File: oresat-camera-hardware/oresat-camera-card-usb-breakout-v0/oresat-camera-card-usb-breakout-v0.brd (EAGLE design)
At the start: 44 x 29 mm, 4 parts, among them J2 USB_A_SMT_FEMALE, J3 2-1734592-0

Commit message: first draft finished
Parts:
- added TP1: TEST-POINTPOGO_PTH, SparkFun-Connectors:1X01_NO_SILK
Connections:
- new net N$2: J3.17, TP1.1
- net GND: no longer J3.17
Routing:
- net N$2: track 0.00 -> 11.3 mm
- net GND: track 19.4 -> 17.4 mm, vias 49 -> 48
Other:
- board text added: "HOST ID"
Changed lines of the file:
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@@
 <text x="8.75" y="7.375" size="1" layer="21" font="vector" ratio="20">CLIENT</text>
 <text x="28.375" y="17.25" size="1" layer="21" font="vector" ratio="20">HOST</text>
+<text x="32.5" y="21.75" size="1" layer="21" font="vector" ratio="20">HOST ID</text>
 </plain>
 <attributes>
@@
 <attribute name="NAME" x="18" y="3" size="0.3" layer="33" ratio="15" rot="R270" align="center"/>
 </element>
+<element name="TP1" library="SparkFun-Connectors" package="1X01_NO_SILK" value="TEST-POINTPOGO_PTH" x="35" y="20" smashed="yes">
+<attribute name="NAME" x="36.48" y="19.768" size="0.6096" layer="25" font="vector" ratio="20"/>
+</element>
 </elements>
 <signals>
@@
 <contactref element="J3" pad="10"/>
 <contactref element="J3" pad="14"/>
-<contactref element="J3" pad="17"/>
 <contactref element="J3" pad="S1"/>
 <contactref element="J3" pad="S2"/>
@@
 <via x="13.875" y="24" extent="1-16" drill="0.35"/>
 <via x="15.625" y="26.125" extent="1-16" drill="0.35"/>
-<via x="25.5" y="23.3125" extent="1-16" drill="0.35"/>
+<via x="25.75" y="23.3125" extent="1-16" drill="0.35"/>
 <via x="26.5" y="23.3125" extent="1-16" drill="0.35"/>
 <via x="28.4375" y="21.75" extent="1-16" drill="0.35"/>
 <via x="30.1875" y="23.9375" extent="1-16" drill="0.35"/>
 <via x="28.4375" y="26" extent="1-16" drill="0.35"/>
-<via x="25.5" y="21.0625" extent="1-16" drill="0.35"/>
 <via x="26.5625" y="21.0625" extent="1-16" drill="0.35"/>
 <via x="32.5625" y="14.3125" extent="1-16" drill="0.35"/>
@@
 <via x="21" y="6" extent="1-16" drill="0.35"/>
 <via x="19" y="9" extent="1-16" drill="0.35"/>
-<via x="31" y="20" extent="1-16" drill="0.35"/>
+<via x="32" y="19" extent="1-16" drill="0.35"/>
 <via x="30" y="10" extent="1-16" drill="0.35"/>
 <via x="30" y="3" extent="1-16" drill="0.35"/>
@@
 <wire x1="26.268" y1="22.225" x2="26.268" y2="23.0805" width="0.254" layer="1"/>
 <wire x1="26.268" y1="23.0805" x2="26.5" y2="23.3125" width="0.254" layer="1"/>
-<wire x1="25.768" y1="22.225" x2="25.768" y2="23.0445" width="0.254" layer="1"/>
-<wire x1="25.768" y1="23.0445" x2="25.5" y2="23.3125" width="0.254" layer="1"/>
-<wire x1="25.268" y1="22.225" x2="25.268" y2="23.0805" width="0.254" layer="1"/>
-<wire x1="25.268" y1="23.0805" x2="25.5" y2="23.3125" width="0.254" layer="1"/>
 <wire x1="21.768" y1="22.225" x2="21.768" y2="23.0805" width="0.254" layer="1"/>
 <wire x1="21.768" y1="23.0805" x2="22" y2="23.3125" width="0.254" layer="1"/>
@@
 <wire x1="12.3" y1="5.6125" x2="12.5" y2="5.8125" width="0.254" layer="1"/>
 <contactref element="C1" pad="1"/>
-<wire x1="25.268" y1="22.225" x2="25.268" y2="21.2945" width="0.254" layer="1"/>
-<wire x1="25.268" y1="21.2945" x2="25.5" y2="21.0625" width="0.254" layer="1"/>
 <wire x1="25.768" y1="22.225" x2="25.768" y2="21.3305" width="0.254" layer="1"/>
-<wire x1="25.768" y1="21.3305" x2="25.5" y2="21.0625" width="0.254" layer="1"/>
 <wire x1="26.268" y1="22.225" x2="26.268" y2="21.357" width="0.254" layer="1"/>
 <wire x1="26.268" y1="21.357" x2="26.5625" y2="21.0625" width="0.254" layer="1"/>
 <wire x1="26.768" y1="22.225" x2="26.768" y2="21.268" width="0.254" layer="1"/>
 <wire x1="26.768" y1="21.268" x2="26.5625" y2="21.0625" width="0.254" layer="1"/>
+<wire x1="25.75" y1="23.3125" x2="25.768" y2="23.2945" width="0.254" layer="1"/>
+<wire x1="25.768" y1="23.2945" x2="25.768" y2="22.225" width="0.254" layer="1"/>
+<wire x1="25.768" y1="21.3305" x2="26.036" y2="21.0625" width="0.254" layer="1"/>
+<wire x1="26.036" y1="21.0625" x2="26.5625" y2="21.0625" width="0.254" layer="1"/>
+<wire x1="33" y1="26" x2="37" y2="26" width="0" layer="19" extent="1-1"/>
+<wire x1="30.1875" y1="23.9375" x2="33" y2="26" width="0" layer="19" extent="1-1"/>
+<wire x1="28.438" y1="23.925" x2="30.1875" y2="23.9375" width="0" layer="19" extent="1-1"/>
+<wire x1="26.5" y1="23.3125" x2="28.438" y2="23.925" width="0" layer="19" extent="1-1"/>
+<wire x1="28.4375" y1="21.75" x2="26.768" y2="22.225" width="0" layer="19" extent="1-1"/>
+<wire x1="23.75" y1="23.3125" x2="25.75" y2="23.3125" width="0" layer="19" extent="1-1"/>
+<wire x1="22.268" y1="22.225" x2="23.768" y2="22.225" width="0" layer="19" extent="1-1"/>
+<wire x1="20.768" y1="22.225" x2="21.768" y2="22.225" width="0" layer="19" extent="1-1"/>
+<wire x1="19.25" y1="23.3125" x2="20.75" y2="23.3125" width="0" layer="19" extent="1-1"/>
+<wire x1="17.768" y1="22.225" x2="19.268" y2="22.225" width="0" layer="19" extent="1-1"/>
+<wire x1="17.375" y1="24.1875" x2="17.5" y2="23.3125" width="0" layer="19" extent="1-1"/>
+<wire x1="15.625" y1="21.8125" x2="17.268" y2="22.225" width="0" layer="19" extent="1-1"/>
+<wire x1="15.598" y1="23.925" x2="17.375" y2="24.1875" width="0" layer="19" extent="1-1"/>
+<wire x1="13.875" y1="24" x2="15.598" y2="23.925" width="0" layer="19" extent="1-1"/>
+<wire x1="28.4375" y1="26" x2="28.438" y2="23.925" width="0" layer="19" extent="1-1"/>
+<wire x1="15.625" y1="26.125" x2="15.598" y2="23.925" width="0" layer="19" extent="1-1"/>
+<wire x1="14" y1="20" x2="15.625" y2="21.8125" width="0" layer="19" extent="1-1"/>
+<wire x1="11.5" y1="17.875" x2="14" y2="20" width="0" layer="19" extent="1-1"/>
+<wire x1="10" y1="16" x2="11.5" y2="17.875" width="0" layer="19" extent="1-1"/>
+<wire x1="11" y1="26" x2="13.875" y2="24" width="0" layer="19" extent="1-1"/>
+<wire x1="8" y1="13" x2="10" y2="16" width="0" layer="19" extent="1-1"/>
+<wire x1="6" y1="12" x2="8" y2="13" width="0" layer="19" extent="1-1"/>
+<wire x1="5" y1="9" x2="6" y2="12" width="0" layer="19" extent="1-1"/>
+<wire x1="3" y1="7" x2="5" y2="9" width="0" layer="19" extent="1-1"/>
+<wire x1="5" y1="6" x2="3" y2="7" width="0" layer="19" extent="1-1"/>
+<wire x1="7" y1="26" x2="11" y2="26" width="0" layer="19" extent="1-1"/>
+<wire x1="3" y1="15" x2="6" y2="12" width="0" layer="19" extent="1-1"/>
+<wire x1="32" y1="19" x2="28.4375" y2="21.75" width="0" layer="19" extent="1-1"/>
+<wire x1="33.5" y1="16.3125" x2="32" y2="19" width="0" layer="19" extent="1-1"/>
+<wire x1="35" y1="17" x2="33.5" y2="16.3125" width="0" layer="19" extent="1-1"/>
+<wire x1="33.5" y1="14.212" x2="33.5" y2="16.3125" width="0" layer="19" extent="1-1"/>
+<wire x1="32.5625" y1="14.3125" x2="33.5" y2="14.212" width="0" layer="19" extent="1-1"/>
+<wire x1="34.5" y1="14.3125" x2="33.5" y2="14.212" width="0" layer="19" extent="1-1"/>
+<wire x1="33.5" y1="12.0625" x2="33.5" y2="14.212" width="0" layer="19" extent="1-1"/>
+<wire x1="36.5659" y1="10" x2="33.5" y2="12.0625" width="0" layer="19" extent="1-1"/>
+<wire x1="30" y1="10" x2="33.5" y2="12.0625" width="0" layer="19" extent="1-1"/>
+<wire x1="41" y1="7" x2="36.5659" y2="10" width="0" layer="19" extent="1-1"/>
+<wire x1="41" y1="22" x2="37" y2="26" width="0" layer="19" extent="1-1"/>
+<wire x1="3" y1="22" x2="7" y2="26" width="0" layer="19" extent="1-1"/>
+<wire x1="41" y1="15" x2="35" y2="17" width="0" layer="19" extent="1-1"/>
+<wire x1="23.4341" y1="10" x2="30" y2="10" width="0" layer="19" extent="1-1"/>
+<wire x1="19" y1="9" x2="23.4341" y2="10" width="0" layer="19" extent="1-1"/>
+<wire x1="18" y1="12" x2="19" y2="9" width="0" layer="19" extent="1-1"/>
+<wire x1="20" y1="14" x2="18" y2="12" width="0" layer="19" extent="1-1"/>
+<wire x1="16" y1="10" x2="18" y2="12" width="0" layer="19" extent="1-1"/>
+<wire x1="14" y1="8" x2="16" y2="10" width="0" layer="19" extent="1-1"/>
+<wire x1="12.5" y1="5.8125" x2="14" y2="8" width="0" layer="19" extent="1-1"/>
+<wire x1="21" y1="6" x2="19" y2="9" width="0" layer="19" extent="1-1"/>
+<wire x1="18" y1="5" x2="21" y2="6" width="0" layer="19" extent="1-1"/>
+<wire x1="18" y1="3.9" x2="18" y2="5" width="0" layer="19" extent="1-1"/>
+<wire x1="30" y1="3" x2="30" y2="10" width="0" layer="19" extent="1-1"/>
 </signal>
 <signal name="CLIENT_VBUS">
@@
 <wire x1="7" y1="1.5" x2="9.8" y2="1.5" width="0" layer="19" extent="1-1"/>
 </signal>
+<signal name="N$2">
+<contactref element="J3" pad="17"/>
+<contactref element="TP1" pad="1"/>
+<wire x1="25.268" y1="22.225" x2="25.3894" y2="22.1036" width="0.1524" layer="1"/>
+<wire x1="25.3894" y1="22.1036" x2="25.3894" y2="21.0812" width="0.1524" layer="1"/>
+<wire x1="25.3894" y1="21.0812" x2="26.4706" y2="20" width="0.1524" layer="1"/>
+<wire x1="26.4706" y1="20" x2="35" y2="20" width="0.1524" layer="1"/>
+</signal>
 </signals>

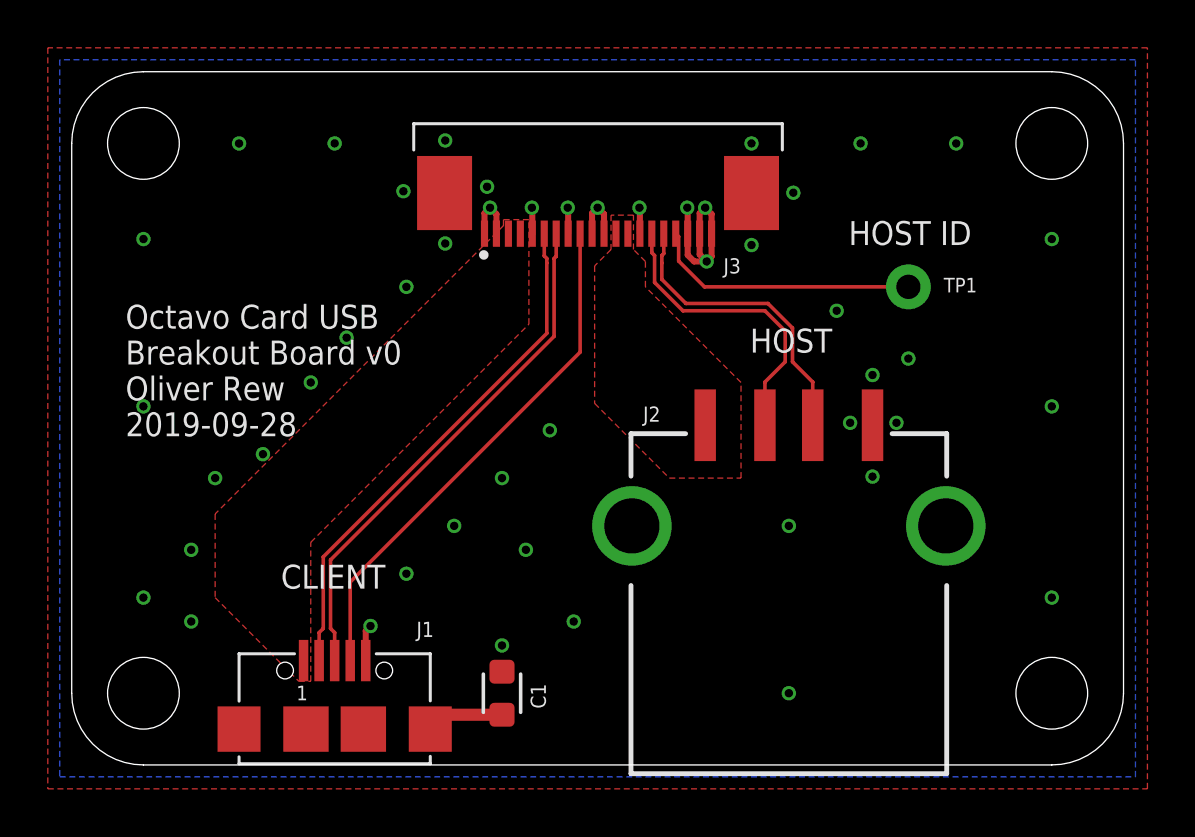
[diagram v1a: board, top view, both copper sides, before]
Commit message: added VDD caps
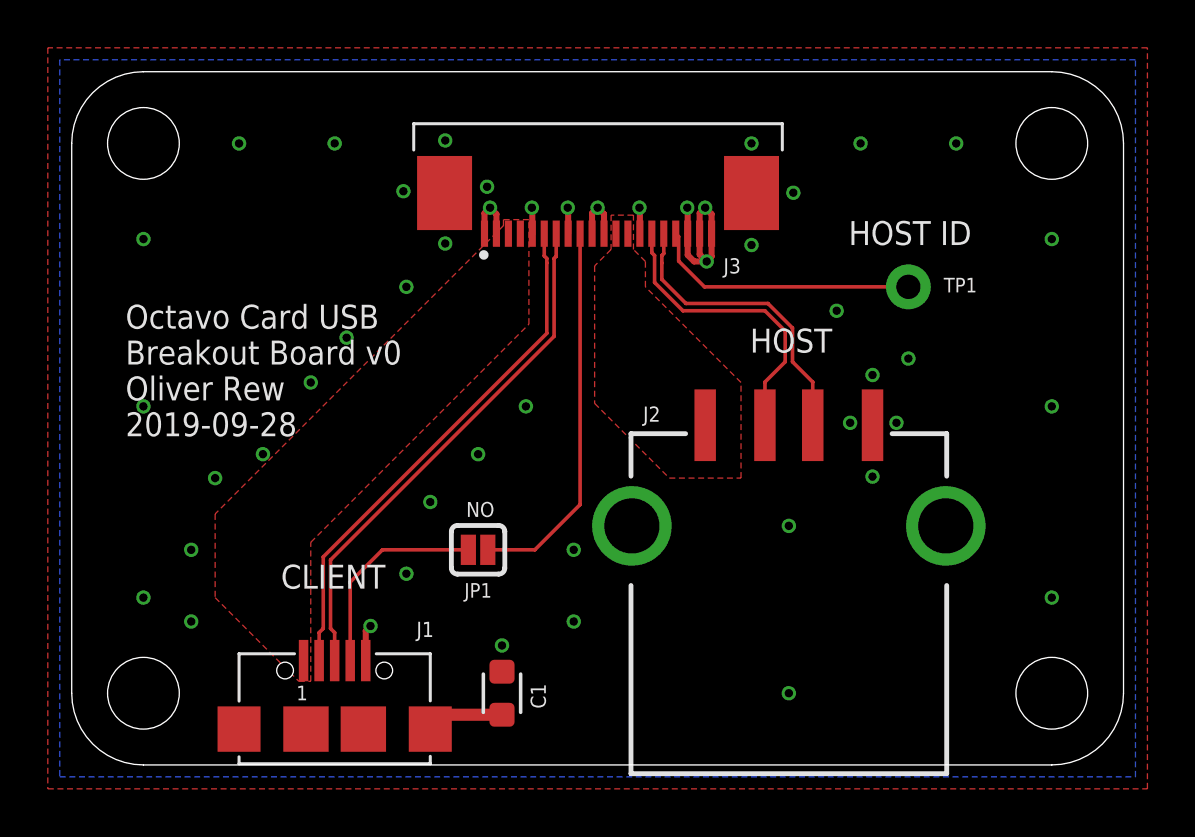
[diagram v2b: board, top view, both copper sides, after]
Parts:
- added JP1: JUMPER-SMT_2_NO_SILK, SparkFun-Jumpers:SMT-JUMPER_2_NO_SILK
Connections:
- new net N$3: J1.4, JP1.2
- net N$5: now also JP1.1; no longer J1.4
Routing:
- net N$3: track 0.00 -> 8.79 mm
- net N$5: track 21.8 -> 16.0 mm
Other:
- board text added: "NO"
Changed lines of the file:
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@@
 <?xml version="1.0" encoding="utf-8"?>
 <!DOCTYPE eagle SYSTEM "eagle.dtd">
-<eagle version="9.5.0">
+<eagle version="9.4.2">
 <drawing>
 <settings>
@@
 <text x="28.375" y="17.25" size="1" layer="21" font="vector" ratio="20">HOST</text>
 <text x="32.5" y="21.75" size="1" layer="21" font="vector" ratio="20">HOST ID</text>
+<text x="16.5" y="10.375" size="0.625" layer="21" font="vector" ratio="20">NO</text>
 </plain>
 <attributes>
@@
 <attribute name="NAME" x="36.48" y="19.768" size="0.6096" layer="25" font="vector" ratio="20"/>
 </element>
+<element name="JP1" library="SparkFun-Jumpers" package="SMT-JUMPER_2_NO_SILK" value="JUMPER-SMT_2_NO_SILK" x="17" y="9" smashed="yes" rot="R180">
+<attribute name="NAME" x="17" y="7.607" size="0.6096" layer="25" font="vector" ratio="20" rot="R180" align="bottom-center"/>
+</element>
 </elements>
 <signals>
@@
 <via x="14" y="20" extent="1-16" drill="0.35"/>
 <via x="14" y="8" extent="1-16" drill="0.35"/>
-<via x="16" y="10" extent="1-16" drill="0.35"/>
-<via x="18" y="12" extent="1-16" drill="0.35"/>
-<via x="20" y="14" extent="1-16" drill="0.35"/>
+<via x="15" y="11" extent="1-16" drill="0.35"/>
+<via x="17" y="13" extent="1-16" drill="0.35"/>
+<via x="19" y="15" extent="1-16" drill="0.35"/>
 <via x="35" y="17" extent="1-16" drill="0.35"/>
 <via x="37" y="26" extent="1-16" drill="0.35"/>
@@
 <via x="18" y="5" extent="1-16" drill="0.35"/>
 <via x="21" y="6" extent="1-16" drill="0.35"/>
-<via x="19" y="9" extent="1-16" drill="0.35"/>
+<via x="21" y="9" extent="1-16" drill="0.35"/>
 <via x="32" y="19" extent="1-16" drill="0.35"/>
 <via x="30" y="10" extent="1-16" drill="0.35"/>
@@
 <wire x1="41" y1="15" x2="35" y2="17" width="0" layer="19" extent="1-1"/>
 <wire x1="23.4341" y1="10" x2="30" y2="10" width="0" layer="19" extent="1-1"/>
-<wire x1="19" y1="9" x2="23.4341" y2="10" width="0" layer="19" extent="1-1"/>
-<wire x1="18" y1="12" x2="19" y2="9" width="0" layer="19" extent="1-1"/>
-<wire x1="20" y1="14" x2="18" y2="12" width="0" layer="19" extent="1-1"/>
-<wire x1="16" y1="10" x2="18" y2="12" width="0" layer="19" extent="1-1"/>
-<wire x1="14" y1="8" x2="16" y2="10" width="0" layer="19" extent="1-1"/>
+<wire x1="21" y1="9" x2="23.4341" y2="10" width="0" layer="19" extent="1-1"/>
+<wire x1="17" y1="13" x2="21" y2="9" width="0" layer="19" extent="1-1"/>
+<wire x1="19" y1="15" x2="17" y2="13" width="0" layer="19" extent="1-1"/>
+<wire x1="15" y1="11" x2="17" y2="13" width="0" layer="19" extent="1-1"/>
+<wire x1="14" y1="8" x2="15" y2="11" width="0" layer="19" extent="1-1"/>
 <wire x1="12.5" y1="5.8125" x2="14" y2="8" width="0" layer="19" extent="1-1"/>
-<wire x1="21" y1="6" x2="19" y2="9" width="0" layer="19" extent="1-1"/>
+<wire x1="21" y1="6" x2="21" y2="9" width="0" layer="19" extent="1-1"/>
 <wire x1="18" y1="5" x2="21" y2="6" width="0" layer="19" extent="1-1"/>
 <wire x1="18" y1="3.9" x2="18" y2="5" width="0" layer="19" extent="1-1"/>
@@
 <signal name="N$5">
 <contactref element="J3" pad="9"/>
-<contactref element="J1" pad="4"/>
-<wire x1="11.65" y1="4.3655" x2="11.65" y2="7.65" width="0.1524" layer="1"/>
-<wire x1="21.268" y1="17.268" x2="21.268" y2="22.225" width="0.1524" layer="1"/>
-<wire x1="11.65" y1="7.65" x2="21.268" y2="17.268" width="0.1524" layer="1"/>
+<contactref element="JP1" pad="1"/>
+<wire x1="17.4064" y1="9" x2="19.375" y2="9" width="0.1524" layer="1"/>
+<wire x1="19.375" y1="9" x2="21.268" y2="10.893" width="0.1524" layer="1"/>
+<wire x1="21.268" y1="10.893" x2="21.268" y2="22.225" width="0.1524" layer="1"/>
 </signal>
 <signal name="HOST_VBUS">
@@
 <wire x1="26.4706" y1="20" x2="35" y2="20" width="0.1524" layer="1"/>
 </signal>
+<signal name="N$3">
+<contactref element="JP1" pad="2"/>
+<contactref element="J1" pad="4"/>
+<wire x1="11.65" y1="4.3655" x2="11.65" y2="7.65" width="0.1524" layer="1"/>
+<wire x1="11.65" y1="7.65" x2="13" y2="9" width="0.1524" layer="1"/>
+<wire x1="13" y1="9" x2="16.5936" y2="9" width="0.1524" layer="1"/>
+</signal>
 </signals>
